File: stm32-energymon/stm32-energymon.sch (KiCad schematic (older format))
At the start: 4 parts, among them J1 Conn_01x14, J2 Conn_01x02, J3 Conn_01x06, U1 blackpill

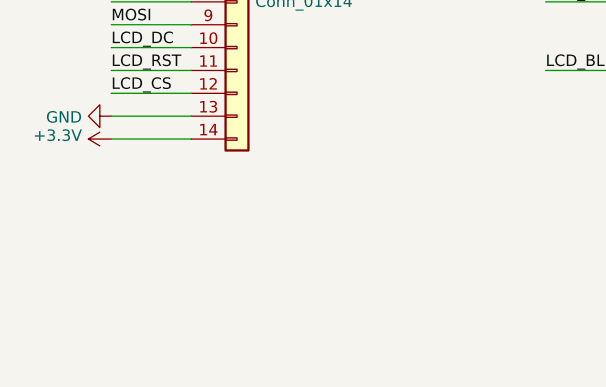
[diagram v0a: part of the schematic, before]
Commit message: Added 1.4" LCD to energymonitor
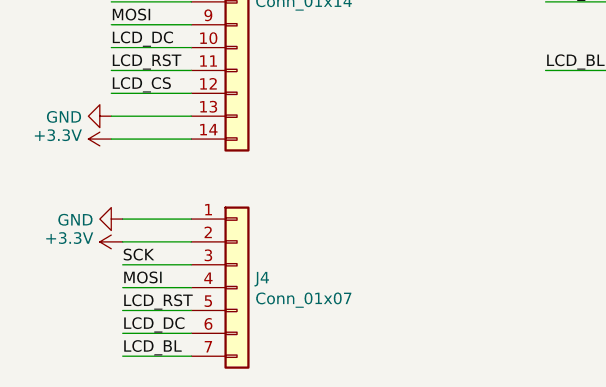
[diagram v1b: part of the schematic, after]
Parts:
- added J4: Conn_01x07, Connector_PinSocket_2.54mm:PinSocket_1x07_P2.54mm_Vertical, symbol Connector_Generic:Conn_01x07
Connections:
- net +3V3: now also J4.2 (Pin_2)
- net GND: now also J4.1 (Pin_1)
- net LCD_BL: now also J4.7 (Pin_7)
- net LCD_DC: now also J4.6 (Pin_6)
- net LCD_RST: now also J4.5 (Pin_5)
- net MOSI: now also J4.4 (Pin_4)
- net SCK: now also J4.3 (Pin_3)
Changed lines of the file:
@@
 Wire Wire Line
 	5050 3400 4750 3400
+$Comp
+L Connector_Generic:Conn_01x07 J4
+U 1 1 5E948F9A
+P 2100 4150
+F 0 "J4" H 2180 4192 50  0000 L CNN
+F 1 "Conn_01x07" H 2180 4101 50  0000 L CNN
+F 2 "Connector_PinSocket_2.54mm:PinSocket_1x07_P2.54mm_Vertical" H 2100 4150 50  0001 C CNN
+F 3 "~" H 2100 4150 50  0001 C CNN
+	1    2100 4150
+	1    0    0    -1
+$EndComp
+Text Label 1600 4050 0    50   ~ 0
+SCK
+Text Label 1600 4150 0    50   ~ 0
+MOSI
+Text Label 1600 4250 0    50   ~ 0
+LCD_RST
+Text Label 1600 4350 0    50   ~ 0
+LCD_DC
+Text Label 1600 4450 0    50   ~ 0
+LCD_BL
+$Comp
+L power:GND #PWR0109
+U 1 1 5E94A771
+P 1600 3850
+F 0 "#PWR0109" H 1600 3600 50  0001 C CNN
+F 1 "GND" V 1605 3722 50  0000 R CNN
+F 2 "" H 1600 3850 50  0001 C CNN
+F 3 "" H 1600 3850 50  0001 C CNN
+	1    1600 3850
+	0    1    1    0
+$EndComp
+$Comp
+L power:+3.3V #PWR0110
+U 1 1 5E94A9A8
+P 1600 3950
+F 0 "#PWR0110" H 1600 3800 50  0001 C CNN
+F 1 "+3.3V" V 1615 4078 50  0000 L CNN
+F 2 "" H 1600 3950 50  0001 C CNN
+F 3 "" H 1600 3950 50  0001 C CNN
+	1    1600 3950
+	0    -1   -1   0
+$EndComp
+Wire Wire Line
+	1600 3850 1900 3850
+Wire Wire Line
+	1600 3950 1900 3950
+Wire Wire Line
+	1600 4050 1900 4050
+Wire Wire Line
+	1600 4150 1900 4150
+Wire Wire Line
+	1600 4250 1900 4250
+Wire Wire Line
+	1600 4350 1900 4350
+Wire Wire Line
+	1600 4450 1900 4450
 $EndSCHEMATC
